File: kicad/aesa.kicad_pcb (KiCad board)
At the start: 4 copper layers, 192 x 315.1 mm, 2139 parts, among them J9501 12 V in (5.5x2.1), J9502 TX power (shunt), J9901 EX_IO1 (AXU3EGB J15), J9902 EX_IO2 (AXU3EGB J16), U1001 OPA1678IDR, U101 OPA1678IDR, U10101 74HCT595D, U10102 UCC27524DR, U10103 UCC27524DR, U10201 74HCT595D, U10202 UCC27524DR, U10203 UCC27524DR, U10301 74HCT595D, U10302 UCC27524DR, U10303 UCC27524DR, U10401 74HCT595D, U10402 UCC27524DR, U10403 UCC27524DR, U10501 74HCT595D, U10502 UCC27524DR, U10503 UCC27524DR, U10601 74HCT595D, U10602 UCC27524DR, U10603 UCC27524DR, U10701 74HCT595D, U10702 UCC27524DR, U10703 UCC27524DR, U10801 74HCT595D, U10802 UCC27524DR, U10803 UCC27524DR, U10901 74HCT595D, U10902 UCC27524DR, U10903 UCC27524DR, U11001 74HCT595D, U11002 UCC27524DR, U11003 UCC27524DR, U1101 OPA1678IDR, U11101 74HCT595D, U11102 UCC27524DR, U11103 UCC27524DR, U11201 74HCT595D, U11202 UCC27524DR, U11203 UCC27524DR, U11301 74HCT595D, U11302 UCC27524DR, U11303 UCC27524DR, U11401 74HCT595D, U11402 UCC27524DR, U11403 UCC27524DR, U11501 74HCT595D, U11502 UCC27524DR, U11503 UCC27524DR, U11601 74HCT595D, U11602 UCC27524DR, U11603 UCC27524DR, U1201 OPA1678IDR, U12101 74AHCT1G125, U12201 74AHCT1G125, U12301 74AHCT1G125, U12401 74AHCT1G125, U1301 OPA1678IDR, U13101 74LVC2G34, U13201 74LVC2G34, U13301 74LVC2G34, U13401 74LVC2G34, U13501 74LVC2G34, U13601 74LVC2G34, U13701 74LVC2G34, U13801 74LVC2G34, U13901 74LVC2G34, U14001 74LVC2G34, U1401 OPA1678IDR, U1501 OPA1678IDR, U1601 OPA1678IDR, U1701 OPA1678IDR, U1801 OPA1678IDR, U1901 OPA1678IDR, U2001 OPA1678IDR, U201 OPA1678IDR, U2101 OPA1678IDR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

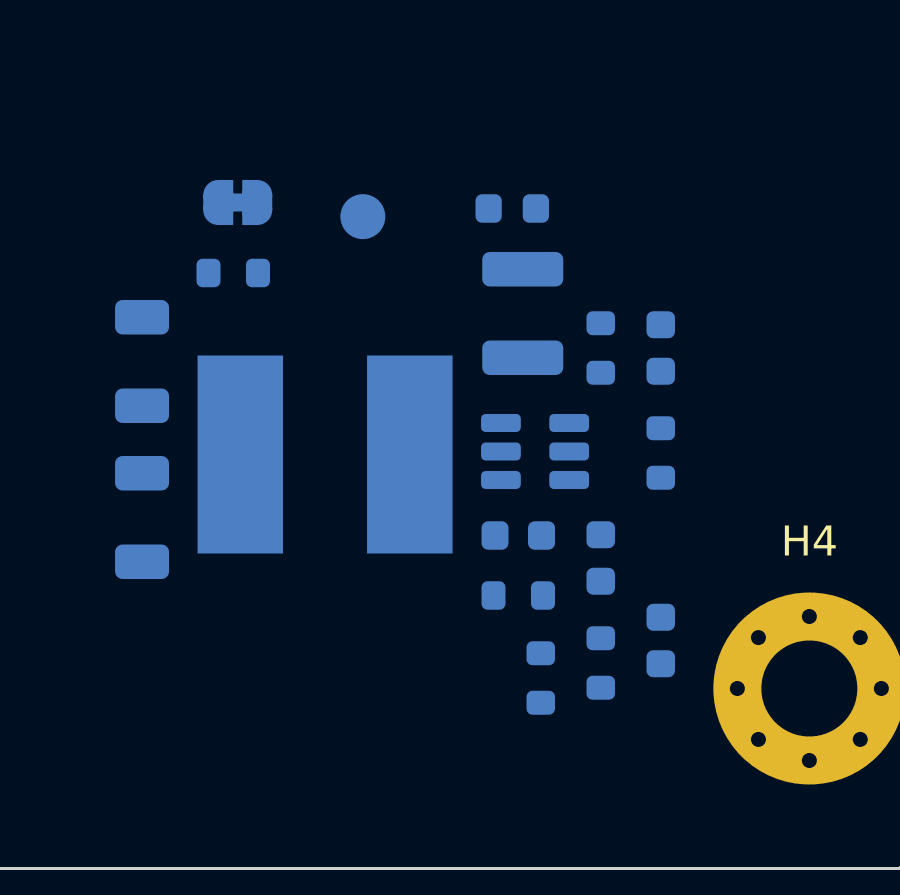
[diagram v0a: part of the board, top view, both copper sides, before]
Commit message: +5V buck hand-routed to the TPS54302 layout guidelines; fixed net-class priorities
- Buck section (place.py POWER_CORES["B"], block_routes.power_buck5v): input caps stacked over VIN with
  shared GND vias and a via at the GND pin; SW 0.6 mm neck then 1 mm into L1, boot cap and DNP snubber
  reaching the switch pad on the back copper (no switching current on the front or under the IC);
  1.6 mm output bar across both output caps; Kelvin FB sense from JP1's regulator side, FB node right of
  the IC away from SW; EN divider beside it; JP1, TP2, R6 and D3 on one +5V line.
- route.py routes section B by hand (POWER_ROUTED A, B, C).
- place.netclasses(): each class gets a fixed priority in list order, so the project file no longer
  changes from one run to the next.

All blocks pass block_check; board DRC has no errors (only the open block ports remain).
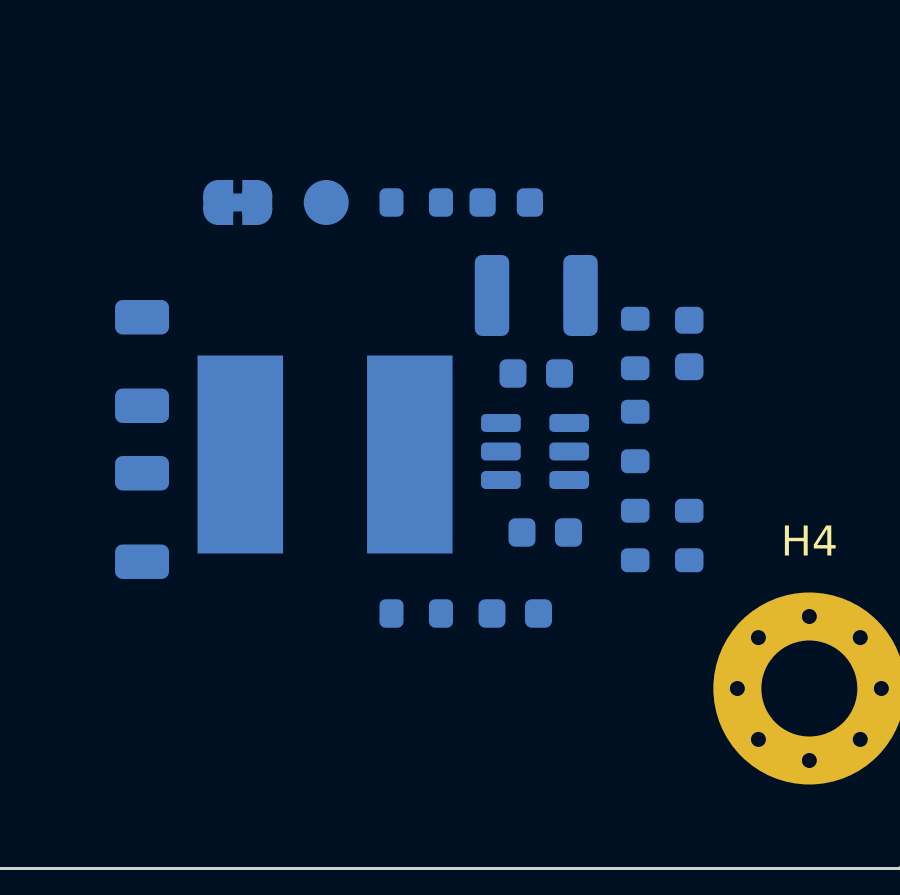
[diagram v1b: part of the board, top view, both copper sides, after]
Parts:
- moved R9503 6.86 mm to (182.0, 304.0)
- moved R9506 6.54 mm to (172.9, 292.9), turned to 0 degrees
- moved R9528 6.37 mm to (172.9, 306.6), turned to 0 degrees
- moved C9504 5.43 mm to (176.9, 298.6)
- moved C9546 4.93 mm to (176.2, 306.6), turned to 0 degrees
- moved R9502 4.38 mm to (180.2, 304.0), turned to -90 degrees
- moved C9505 2.04 mm to (177.2, 303.9), turned to 180 degrees
- moved TP9502 1.31 mm to (169.9, 292.9)
- moved R9504 1.16 mm to (180.2, 297.6)
- moved R9505 1.01 mm to (180.2, 300.7)
- moved C9508 0.96 mm to (182.0, 297.6)
- moved C9503 0.75 mm to (176.9, 296.0), turned to 0 degrees
- moved D9503 0.28 mm to (175.9, 292.9)
